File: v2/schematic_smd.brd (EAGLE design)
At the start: 47 x 39.4 mm, 16 parts, among them J2 DCJ0202, U1 328P

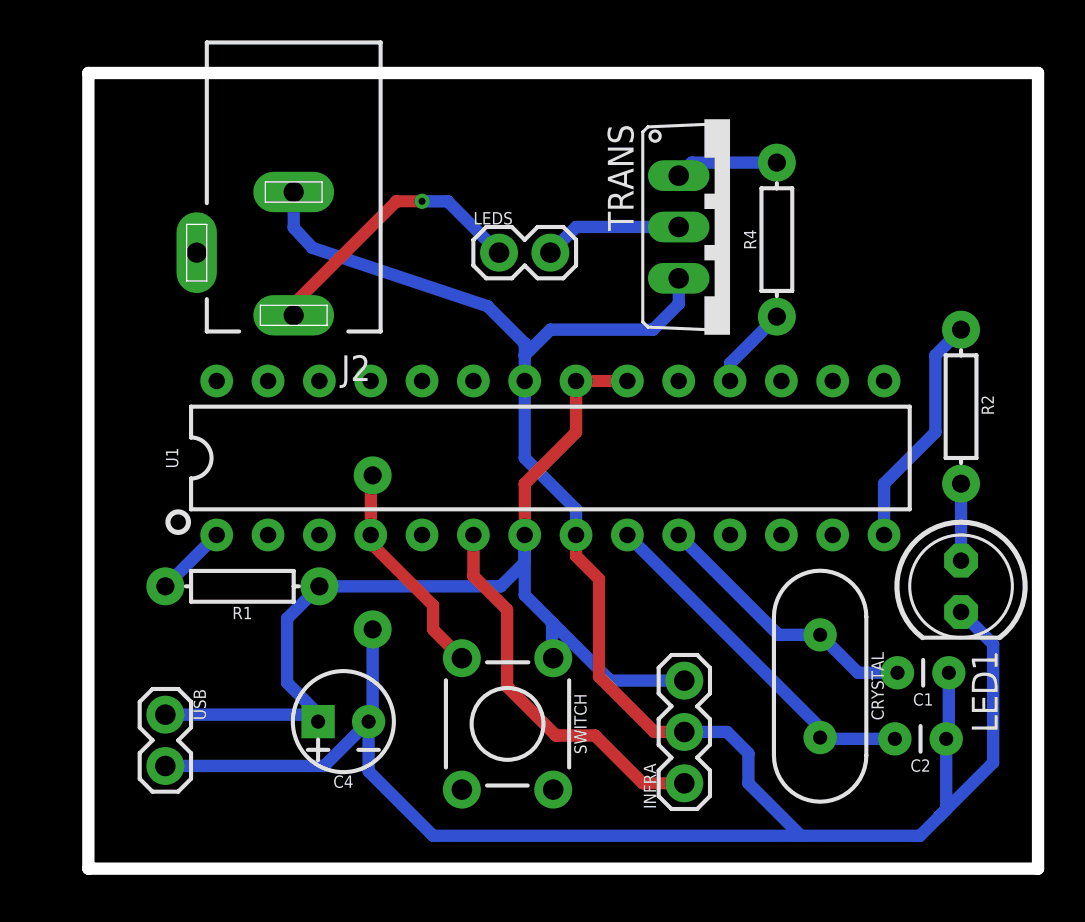
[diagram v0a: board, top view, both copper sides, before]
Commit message: Added v2 smd board
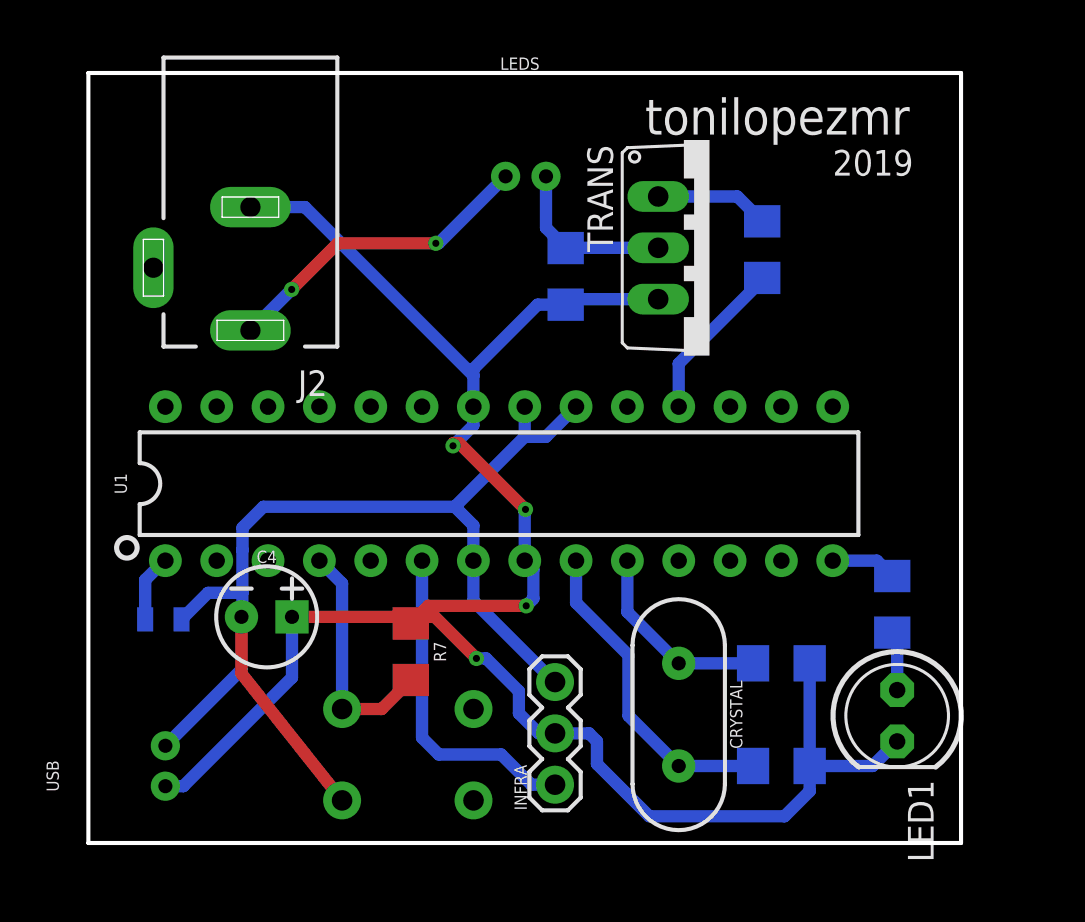
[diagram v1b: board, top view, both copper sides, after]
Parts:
- removed C2: 22pF, SparkFun-Capacitors:CAP-PTH-2.54
- removed R1: 10k, SparkFun-Resistors:AXIAL-0.3
- removed R2, R3: 220, SparkFun-Resistors:AXIAL-0.3
- removed R4: 470ohm, SparkFun-Resistors:AXIAL-0.3
- added C3, C5: 22pF, SparkFun-Capacitors:1206
- added R5: 10k, SparkFun-Resistors:0805
- added R6: 1k, SparkFun-Resistors:1206
- added R7, R8: 470, SparkFun-Resistors:1206
- C1: value 22pF -> 1uF; device SparkFun-Capacitors:CAP-PTH-2.54 -> SparkFun-Capacitors:1206
- LEDS: value (none) -> Leds; device SparkFun-Connectors:1X02 -> SparkFun-Connectors:JST-2-PTH-KIT
- USB: device SparkFun-Connectors:1X02 -> SparkFun-Connectors:JST-2-PTH-KIT
- moved C1 26.4 mm to (23.6, 28.0), flipped to the bottom, turned to 270 degrees
- moved LED1 7.14 mm to (40.0, 6.30)
- moved CRYSTAL 7.14 mm to (29.2, 6.35)
- moved C4 6.42 mm to (8.82, 11.2), turned to 0 degrees
- moved INFRA 6.40 mm to (23.1, 2.88)
- moved SWITCH 5.17 mm to (15.8, 4.37), flipped to the bottom, turned to 180 degrees
- moved LEDS 4.00 mm to (21.6, 33.0)
- moved U1 2.84 mm to (20.3, 17.8)
- moved USB 2.54 mm to (3.81, 3.81), turned to 90 degrees
- moved J2 2.27 mm to (8.02, 28.5)
- moved TRANS 1.45 mm to (30.7, 29.4)
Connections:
- net 12VO: now also C1.1
- net GND: now also C1.2, C3.1, C4.1, C5.1, R7.1, USB.1; no longer C1.1, C2.1, C4.2, R3.P$1, USB.2
- net N$1: now also C5.2; no longer C1.2
- net N$2: now also C3.2; no longer C2.2
- net N$3: now also R6.2; no longer R2.P$2
- net N$4: now also R8.2; no longer R4.P$2
- net PIN12: now also R8.1; no longer R4.P$1
- net PIN2: now also R7.2; no longer R3.P$2
- net PIN8: now also R6.1; no longer R2.P$1
- net RESET: now also R5.2; no longer R1.P$2
- net VCC: now also C4.2, R5.1, USB.2; no longer C4.1, R1.P$1, USB.1
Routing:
- net GND: track 125.1 -> 100.6 mm, vias 0 -> 4
- net PIN8: track 11.7 -> 3.26 mm
- net VCC: track 53.6 -> 58.1 mm
- net N$1: track 13.6 -> 9.81 mm
- net PIN12: track 4.30 -> 8.08 mm
- net PIN4: track 18.9 -> 16.3 mm
- net 12VIN: track 13.9 -> 15.8 mm, vias 1 -> 2
- net N$2: track 17.8 -> 15.9 mm
- net 12VO: track 6.88 -> 8.53 mm
- net N$3: track 3.81 -> 2.94 mm
- net PIN2: track 11.1 -> 11.8 mm
- net N$4: track 5.12 -> 5.66 mm
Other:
- board size 47 x 39.4 mm -> 43.2 x 38.1 mm
- board text removed: "TV Lights"
- board text removed: "v2"
